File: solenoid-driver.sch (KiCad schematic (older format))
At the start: 60 parts, among them Q10 NPN, Q11 DUAL_MOSFET_N, Q12 NPN, Q13 NPN, Q14 DUAL_MOSFET_N, Q15 NPN, Q16 NPN, Q5 DUAL_MOSFET_N, Q6 NPN, Q7 NPN, Q8 DUAL_MOSFET_N, Q9 NPN

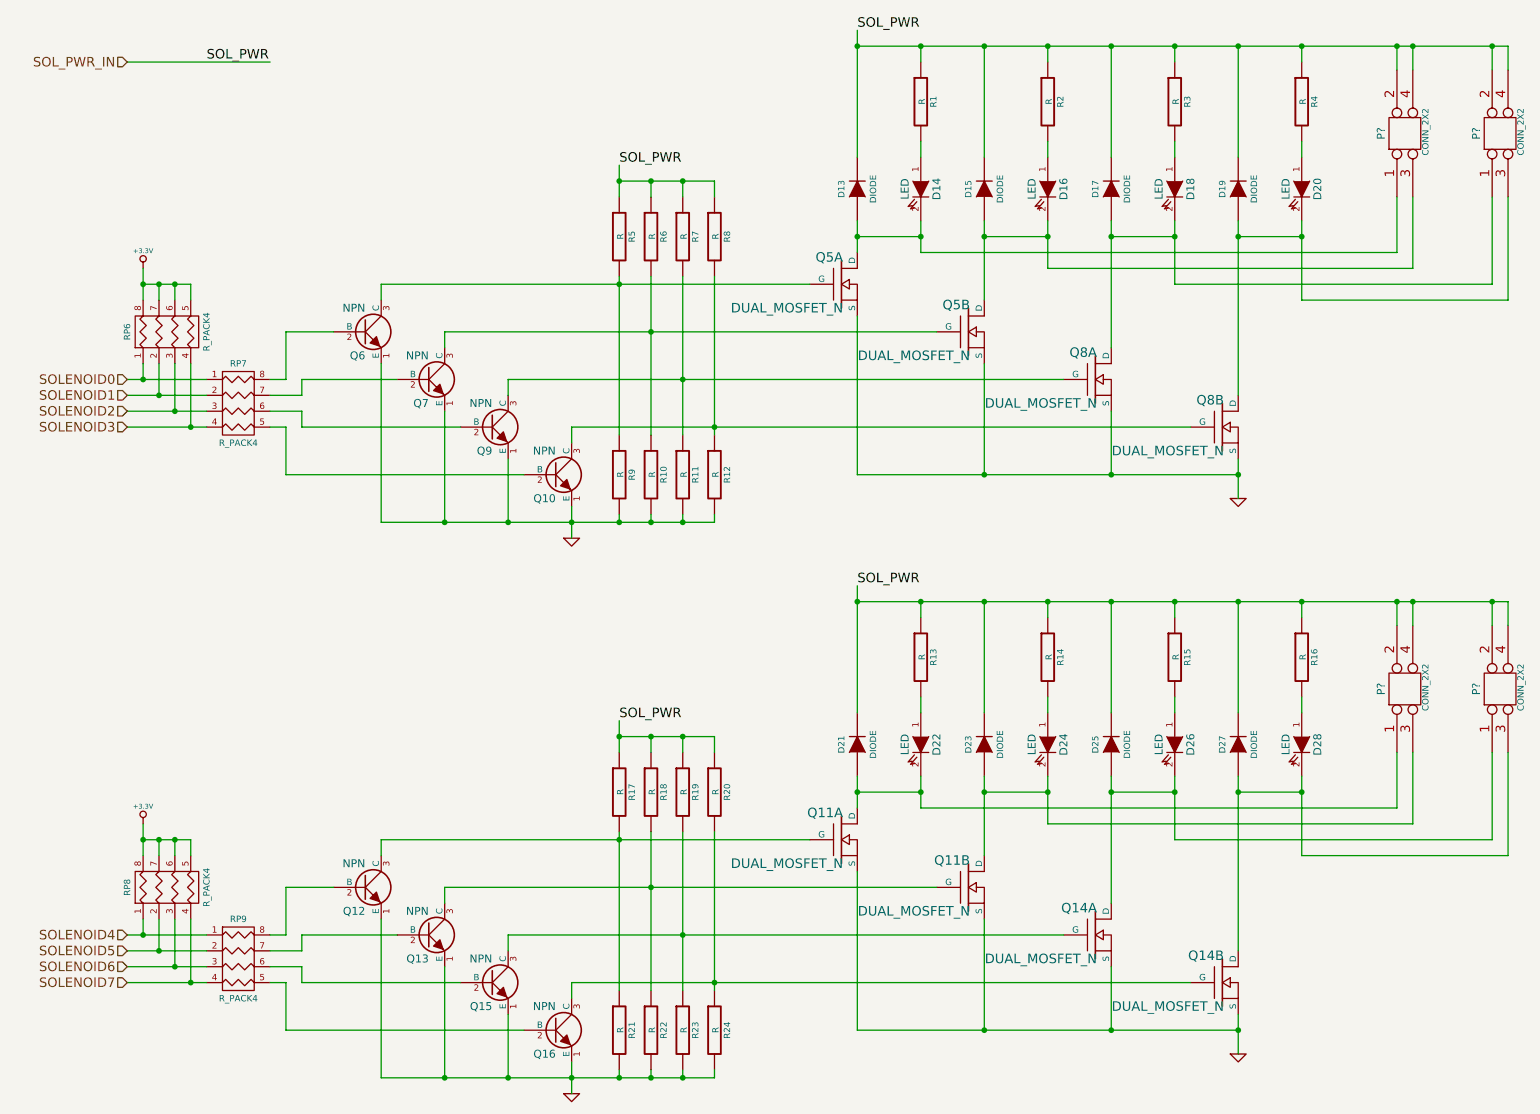
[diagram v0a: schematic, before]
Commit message: changed the controller adding some shift registers
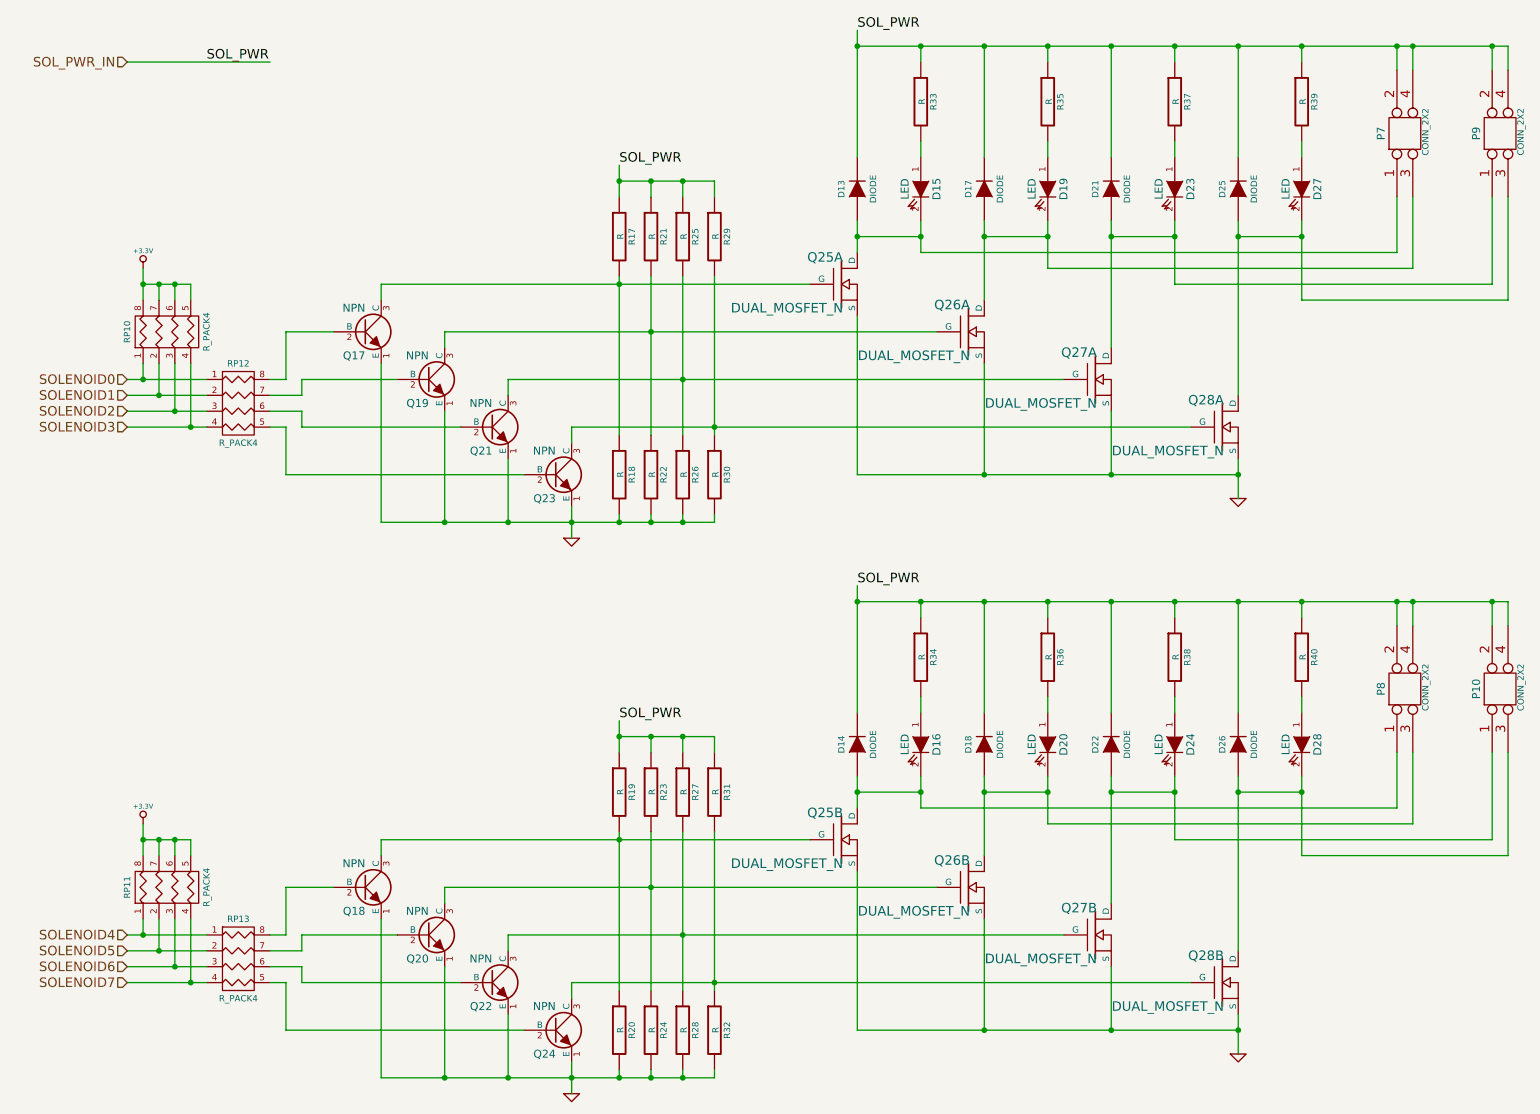
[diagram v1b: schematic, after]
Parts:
- gave numbers to parts that had none: 4
- renumbered D21 to D14, D14 to D15, D22 to D16, D15 to D17, D23 to D18, D16 to D19, D24 to D20, D17 to D21, D25 to D22, D18 to D23, D26 to D24, D19 to D25, D27 to D26, D20 to D27, Q6 to Q17, Q12 to Q18, Q7 to Q19, Q13 to Q20, Q9 to Q21, Q15 to Q22, Q10 to Q23, Q16 to Q24, Q11 to Q25, Q5 to Q25, Q11 to Q26, Q5 to Q26, Q14 to Q27, Q8 to Q27, Q14 to Q28, Q8 to Q28, R5 to R17, R9 to R18, R17 to R19, R21 to R20, R6 to R21, R10 to R22, R18 to R23, R22 to R24, R7 to R25, R11 to R26, R19 to R27, R23 to R28, R8 to R29, R12 to R30, R20 to R31, R24 to R32, R1 to R33, R13 to R34, R2 to R35, R14 to R36, R3 to R37, R15 to R38, R4 to R39, R16 to R40, RP6 to RP10, RP8 to RP11, RP7 to RP12, RP9 to RP13
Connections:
- net GND: now also Q25.S2 (S), Q26.S1 (S), Q27.S2 (S), Q28.S1 (S); no longer Q25.S1 (S), Q26.S2 (S), Q27.S1 (S), Q28.S2 (S)
- net at Q18.3 (C), R19.2, R20.1: now also Q25.G2 (G); no longer Q25.G1 (G)
- net at D14.1 (A), D16.2 (K), P8.1: now also Q25.D2 (D); no longer Q25.D1 (D)
- net at Q22.3 (C), R27.2, R28.1: now also Q27.G2 (G); no longer Q27.G1 (G)
- net at D22.1 (A), D24.2 (K), P10.1: now also Q27.D2 (D); no longer Q27.D1 (D)
- net at Q19.3 (C), R21.2, R22.1: now also Q26.G1 (G); no longer Q26.G2 (G)
- net at Q23.3 (C), R29.2, R30.1: now also Q28.G1 (G); no longer Q28.G2 (G)
- net at D17.1 (A), D19.2 (K), P7.3: now also Q26.D1 (D); no longer Q26.D2 (D)
- net at D25.1 (A), D27.2 (K), P9.3: now also Q28.D1 (D); no longer Q28.D2 (D)

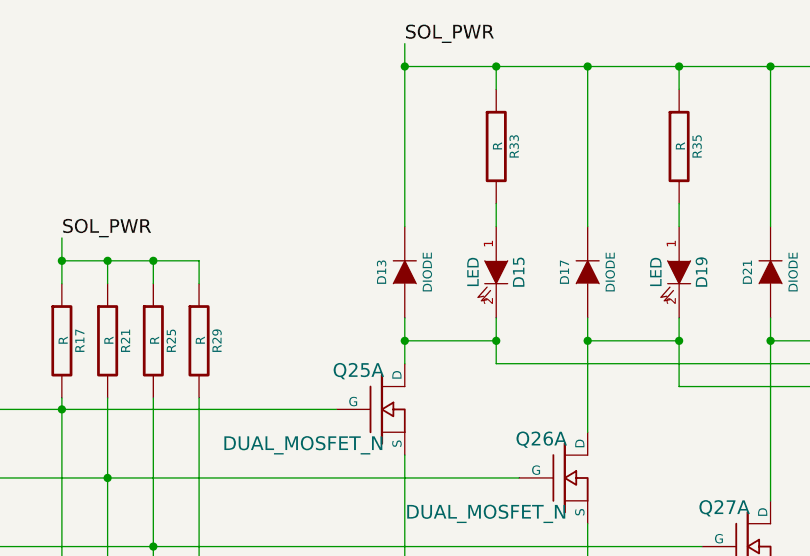
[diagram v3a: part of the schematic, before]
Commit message: added some more info to the different components, changed the pinout for zeeners, and am hating ki-cad for schematic to pads.
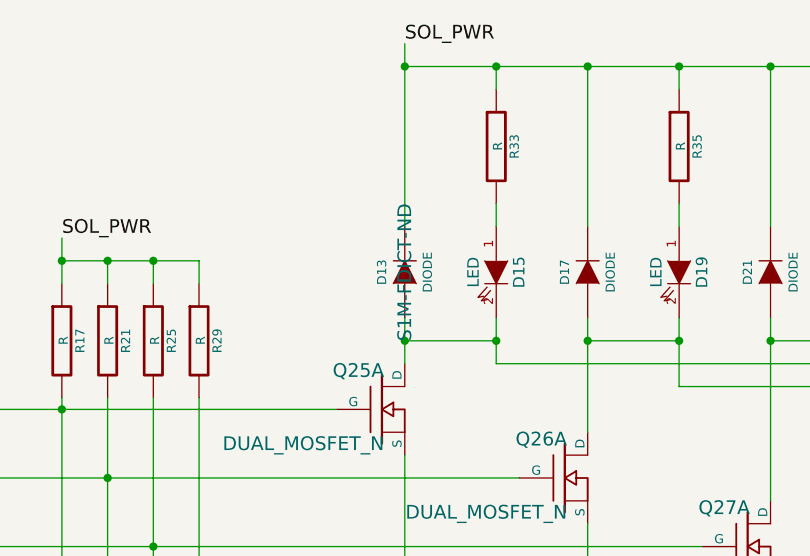
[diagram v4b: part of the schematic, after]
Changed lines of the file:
@@
-EESchema Schematic File Version 2  date 4/18/2013 1:12:38 AM
+EESchema Schematic File Version 2  date 4/19/2013 12:46:09 AM
 LIBS:power
 LIBS:device
@@
 Sheet 4 10
 Title ""
-Date "18 apr 2013"
+Date "19 apr 2013"
 Rev ""
 Comp ""
@@
 F 1 "DIODE" H 6000 1600 40  0000 C CNN
 F 2 "~" H 6000 1700 60  0000 C CNN
-F 3 "~" H 6000 1700 60  0000 C CNN
+F 3 "S1M-FDICT-ND" H 6000 1700 60  0000 C CNN
 	1    6000 1700
 	0    -1   -1   0
